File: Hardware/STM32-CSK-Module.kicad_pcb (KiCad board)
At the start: 2 copper layers, 7 parts

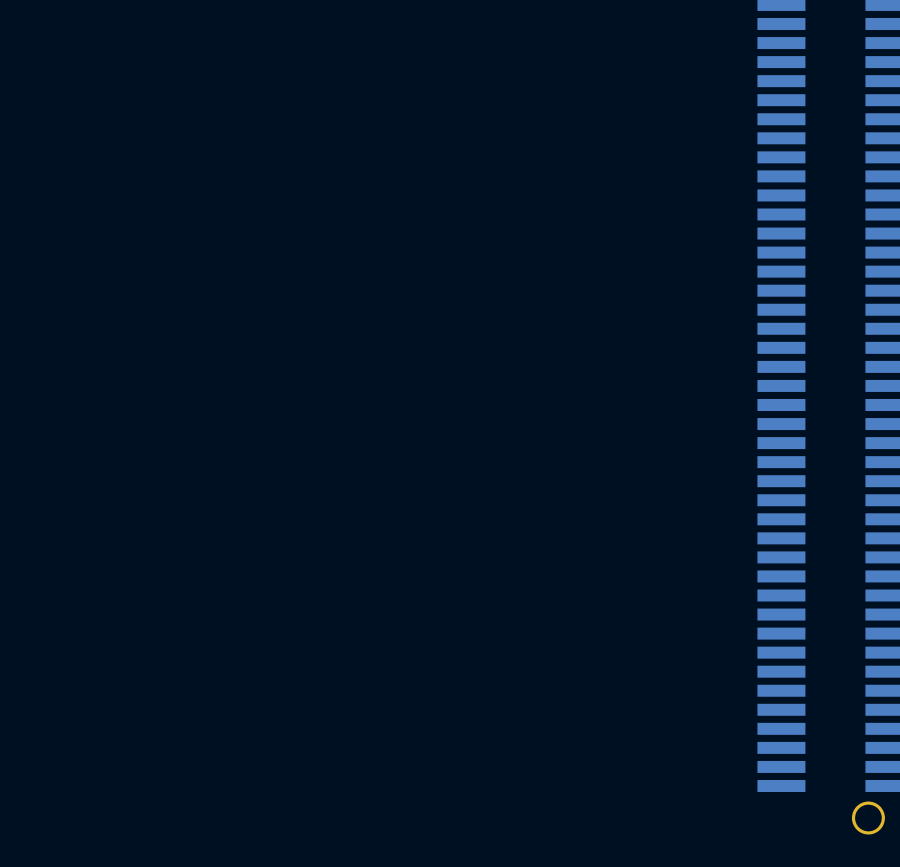
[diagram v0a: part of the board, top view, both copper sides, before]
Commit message: Add MCU
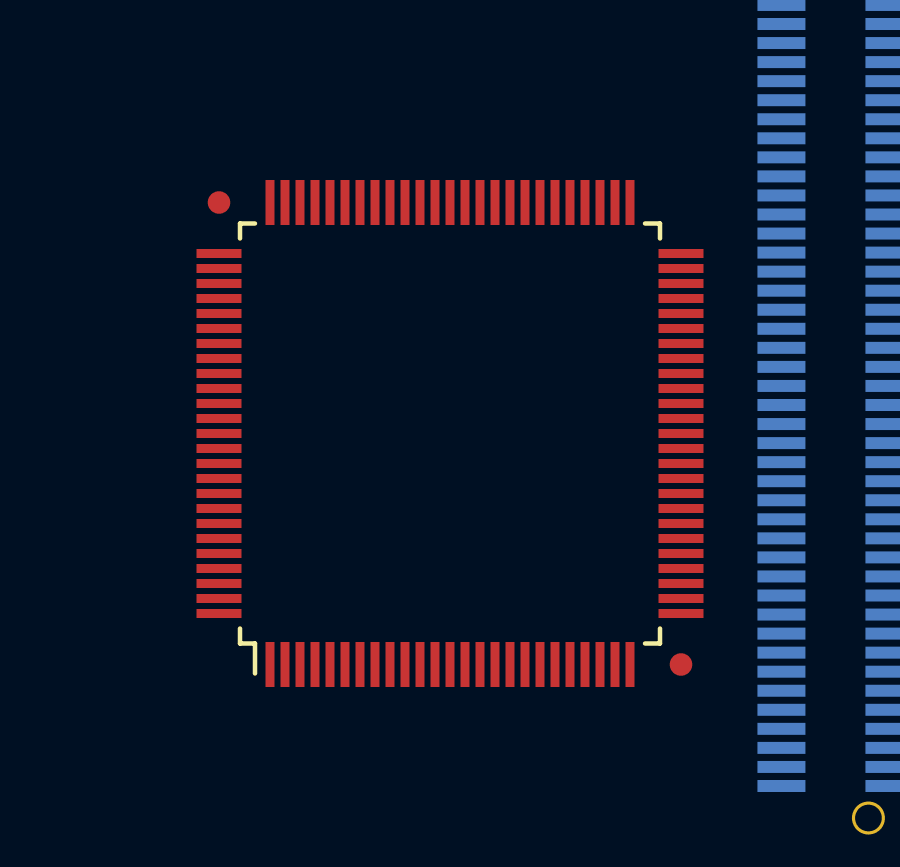
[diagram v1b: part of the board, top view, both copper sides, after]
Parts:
- added U1: STM32F4X7V, QFP50P1600X1600-100N, F.Cu at (209.0, 120.0)
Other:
- board text added: "Connector keep out"

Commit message: Migrate to new KiCad
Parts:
- added C1: 0.1uF, Capacitors:CAPC1608N, F.Cu at (208.4, 156.5)
- added C10: 0.1uF, Capacitors:CAPC1608N, F.Cu at (222.8, 156.5)
- added C11: 2.2uF, Capacitors:CAPC1608N, F.Cu at (216.9, 161.7)
- added C12: 0.1uF, Capacitors:CAPC1608N, F.Cu at (213.2, 166.9)
- added C13: 0.1uF, Capacitors:CAPC1608N, F.Cu at (221.7, 161.7)
- added C2: 0.1uF, Capacitors:CAPC1608N, F.Cu at (213.9, 151.3)
- added C3: 1uF, Capacitors:CAPC1608N, F.Cu at (207.8, 161.7)
- added C4: 4.7uF, Capacitors:CAPC1608N, F.Cu at (218.7, 151.3)
- added C5: 0.1uF, Capacitors:CAPC1608N, F.Cu at (213.2, 156.5)
- added C6: 0.1uF, Capacitors:CAPC1608N, F.Cu at (208.4, 166.9)
- added C7: 0.1uF, Capacitors:CAPC1608N, F.Cu at (218.0, 156.5)
- added C8: 0.1uF, Capacitors:CAPC1608N, F.Cu at (212.1, 161.7)
- added C9: 2.2uF, Capacitors:CAPC1608N, F.Cu at (223.5, 151.3)
- added FB1: Ferrite, Inductors:INDC1608N, F.Cu at (208.8, 151.3)
- added R1: 10k, Resistors:RESC1608N, F.Cu at (217.4, 166.9)
- H1: value CUBESAT-PSPM -> Conn_Cubesat-PPM; footprint CONN-LSS-150 -> Connectors:Conn_Samtec-LSS-150
- MECH-HOLE220 (x6): footprint MECH-HOLE220 -> Mechanical:MTGP575H254
- U1: value STM32F4X7V -> STM32F417VGT; footprint QFP50P1600X1600-100N -> QFP:QFP50P1600X1600-100N
- moved U1 39.5 mm to (197.0, 157.6)
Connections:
- H1 pad 1: (no net) -> Net-(H1-Pad1)
- H1 pad 10: (no net) -> Net-(H1-Pad10)
- H1 pad 100: (no net) -> Net-(H1-Pad100)
- H1 pad 11: (no net) -> Net-(H1-Pad11)
- H1 pad 12: (no net) -> Net-(H1-Pad12)
- H1 pad 13: (no net) -> Net-(H1-Pad13)
- H1 pad 14: (no net) -> Net-(H1-Pad14)
- H1 pad 15: (no net) -> Net-(H1-Pad15)
- H1 pad 16: (no net) -> Net-(H1-Pad16)
- H1 pad 17: (no net) -> Net-(H1-Pad17)
- H1 pad 18: (no net) -> Net-(H1-Pad18)
- H1 pad 19: (no net) -> Net-(H1-Pad19)
- H1 pad 2: (no net) -> Net-(H1-Pad2)
- H1 pad 20: (no net) -> Net-(H1-Pad20)
- H1 pad 21: (no net) -> Net-(H1-Pad21)
- H1 pad 22: (no net) -> Net-(H1-Pad22)
- H1 pad 23: (no net) -> Net-(H1-Pad23)
- H1 pad 24: (no net) -> Net-(H1-Pad24)
- H1 pad 25: (no net) -> Net-(H1-Pad25)
- H1 pad 26: (no net) -> Net-(H1-Pad26)
- H1 pad 27: (no net) -> Net-(H1-Pad27)
- H1 pad 28: (no net) -> Net-(H1-Pad28)
- H1 pad 29: (no net) -> Net-(H1-Pad29)
- H1 pad 3: (no net) -> Net-(H1-Pad3)
- H1 pad 30: (no net) -> Net-(H1-Pad30)
- H1 pad 31: (no net) -> Net-(H1-Pad31)
- H1 pad 32: (no net) -> Net-(H1-Pad32)
- H1 pad 33: (no net) -> Net-(H1-Pad33)
- H1 pad 34: (no net) -> Net-(H1-Pad34)
- H1 pad 35: (no net) -> Net-(H1-Pad35)
- H1 pad 36: (no net) -> Net-(H1-Pad36)
- H1 pad 37: (no net) -> Net-(H1-Pad37)
- H1 pad 38: (no net) -> Net-(H1-Pad38)
- H1 pad 39: (no net) -> Net-(H1-Pad39)
- H1 pad 4: (no net) -> Net-(H1-Pad4)
- H1 pad 40: (no net) -> Net-(H1-Pad40)
- H1 pad 41: (no net) -> Net-(H1-Pad41)
- H1 pad 42: (no net) -> Net-(H1-Pad42)
- H1 pad 43: (no net) -> Net-(H1-Pad43)
- H1 pad 44: (no net) -> Net-(H1-Pad44)
- H1 pad 45: (no net) -> Net-(H1-Pad45)
- H1 pad 46: (no net) -> Net-(H1-Pad46)
- H1 pad 47: (no net) -> Net-(H1-Pad47)
- H1 pad 48: (no net) -> Net-(H1-Pad48)
- H1 pad 49: (no net) -> Net-(H1-Pad49)
- H1 pad 5: (no net) -> Net-(H1-Pad5)
- H1 pad 50: (no net) -> Net-(H1-Pad50)
- H1 pad 51: (no net) -> Net-(H1-Pad51)
- H1 pad 52: (no net) -> Net-(H1-Pad52)
- H1 pad 53: (no net) -> Net-(H1-Pad53)
- H1 pad 54: (no net) -> Net-(H1-Pad54)
- H1 pad 55: (no net) -> Net-(H1-Pad55)
- H1 pad 56: (no net) -> Net-(H1-Pad56)
- H1 pad 57: (no net) -> GND
- H1 pad 58: (no net) -> GND
- H1 pad 59: (no net) -> Net-(H1-Pad59)
- H1 pad 6: (no net) -> Net-(H1-Pad6)
- H1 pad 60: (no net) -> Net-(H1-Pad60)
- H1 pad 61: (no net) -> Net-(H1-Pad61)
- H1 pad 62: (no net) -> Net-(H1-Pad62)
- H1 pad 63: (no net) -> Net-(H1-Pad63)
- H1 pad 64: (no net) -> Net-(H1-Pad64)
- H1 pad 65: (no net) -> Net-(H1-Pad65)
- H1 pad 66: (no net) -> Net-(H1-Pad66)
- H1 pad 67: (no net) -> Net-(H1-Pad67)
- H1 pad 68: (no net) -> Net-(H1-Pad68)
- H1 pad 69: (no net) -> Net-(H1-Pad69)
- H1 pad 7: (no net) -> Net-(H1-Pad7)
- H1 pad 70: (no net) -> Net-(H1-Pad70)
- H1 pad 71: (no net) -> Net-(H1-Pad71)
- H1 pad 72: (no net) -> Net-(H1-Pad72)
- H1 pad 73: (no net) -> Net-(H1-Pad73)
- H1 pad 74: (no net) -> Net-(H1-Pad74)
- H1 pad 75: (no net) -> Net-(H1-Pad75)
- H1 pad 76: (no net) -> Net-(H1-Pad76)
- H1 pad 77: (no net) -> Net-(H1-Pad77)
- H1 pad 78: (no net) -> Net-(H1-Pad78)
- H1 pad 79: (no net) -> Net-(H1-Pad79)
- H1 pad 8: (no net) -> Net-(H1-Pad8)
- H1 pad 80: (no net) -> Net-(H1-Pad80)
- H1 pad 81: (no net) -> Net-(H1-Pad81)
- H1 pad 82: (no net) -> Net-(H1-Pad82)
- H1 pad 83: (no net) -> Net-(H1-Pad83)
- H1 pad 84: (no net) -> Net-(H1-Pad84)
- H1 pad 85: (no net) -> Net-(H1-Pad85)
- H1 pad 86: (no net) -> Net-(H1-Pad86)
- H1 pad 87: (no net) -> Net-(H1-Pad87)
- H1 pad 88: (no net) -> Net-(H1-Pad88)
- H1 pad 89: (no net) -> Net-(H1-Pad89)
- H1 pad 9: (no net) -> Net-(H1-Pad9)
- H1 pad 90: (no net) -> Net-(H1-Pad90)
- H1 pad 91: (no net) -> Net-(H1-Pad91)
- H1 pad 92: (no net) -> Net-(H1-Pad92)
- H1 pad 93: (no net) -> Net-(H1-Pad93)
- H1 pad 94: (no net) -> Net-(H1-Pad94)
- H1 pad 95: (no net) -> Net-(H1-Pad95)
- H1 pad 96: (no net) -> Net-(H1-Pad96)
- H1 pad 97: (no net) -> Net-(H1-Pad97)
- H1 pad 98: (no net) -> Net-(H1-Pad98)
- H1 pad 99: (no net) -> Net-(H1-Pad99)
- U1 pad 1: (no net) -> Net-(U1-Pad1)
- U1 pad 10: (no net) -> GND
- U1 pad 100: (no net) -> +3V3
- U1 pad 11: (no net) -> +3V3
- U1 pad 12: (no net) -> Net-(U1-Pad12)
- U1 pad 13: (no net) -> Net-(U1-Pad13)
- U1 pad 14: (no net) -> /~RST
- U1 pad 15: (no net) -> Net-(U1-Pad15)
- U1 pad 16: (no net) -> Net-(U1-Pad16)
- U1 pad 17: (no net) -> Net-(U1-Pad17)
- U1 pad 18: (no net) -> Net-(U1-Pad18)
- U1 pad 19: (no net) -> +3V3
- U1 pad 2: (no net) -> Net-(U1-Pad2)
- U1 pad 20: (no net) -> GND
- U1 pad 21: (no net) -> /VDDA
- U1 pad 22: (no net) -> /VDDA
- U1 pad 23: (no net) -> Net-(U1-Pad23)
- U1 pad 24: (no net) -> Net-(U1-Pad24)
- U1 pad 25: (no net) -> Net-(U1-Pad25)
- U1 pad 26: (no net) -> Net-(U1-Pad26)
- U1 pad 27: (no net) -> GND
- U1 pad 28: (no net) -> +3V3
- U1 pad 29: (no net) -> Net-(U1-Pad29)
- U1 pad 3: (no net) -> Net-(U1-Pad3)
- U1 pad 30: (no net) -> Net-(U1-Pad30)
- U1 pad 31: (no net) -> Net-(U1-Pad31)
- U1 pad 32: (no net) -> Net-(U1-Pad32)
- U1 pad 33: (no net) -> Net-(U1-Pad33)
- U1 pad 34: (no net) -> Net-(U1-Pad34)
- U1 pad 35: (no net) -> Net-(U1-Pad35)
- U1 pad 36: (no net) -> Net-(U1-Pad36)
- U1 pad 37: (no net) -> Net-(U1-Pad37)
- U1 pad 38: (no net) -> Net-(U1-Pad38)
- U1 pad 39: (no net) -> Net-(U1-Pad39)
- U1 pad 4: (no net) -> Net-(U1-Pad4)
- U1 pad 40: (no net) -> Net-(U1-Pad40)
- U1 pad 41: (no net) -> Net-(U1-Pad41)
- U1 pad 42: (no net) -> Net-(U1-Pad42)
- U1 pad 43: (no net) -> Net-(U1-Pad43)
- U1 pad 44: (no net) -> Net-(U1-Pad44)
- U1 pad 45: (no net) -> Net-(U1-Pad45)
- U1 pad 46: (no net) -> Net-(U1-Pad46)
- U1 pad 47: (no net) -> Net-(U1-Pad47)
- U1 pad 48: (no net) -> Net-(U1-Pad48)
- U1 pad 49: (no net) -> /VCAP1
- U1 pad 5: (no net) -> Net-(U1-Pad5)
- U1 pad 50: (no net) -> +3V3
- U1 pad 51: (no net) -> Net-(U1-Pad51)
- U1 pad 52: (no net) -> Net-(U1-Pad52)
- U1 pad 53: (no net) -> Net-(U1-Pad53)
- U1 pad 54: (no net) -> Net-(U1-Pad54)
- U1 pad 55: (no net) -> Net-(U1-Pad55)
- U1 pad 56: (no net) -> Net-(U1-Pad56)
- U1 pad 57: (no net) -> Net-(U1-Pad57)
- U1 pad 58: (no net) -> Net-(U1-Pad58)
- U1 pad 59: (no net) -> Net-(U1-Pad59)
- U1 pad 6: (no net) -> /VBAT
- U1 pad 60: (no net) -> Net-(U1-Pad60)
- U1 pad 61: (no net) -> Net-(U1-Pad61)
- U1 pad 62: (no net) -> Net-(U1-Pad62)
- U1 pad 63: (no net) -> Net-(U1-Pad63)
- U1 pad 64: (no net) -> Net-(U1-Pad64)
- U1 pad 65: (no net) -> Net-(U1-Pad65)
- U1 pad 66: (no net) -> Net-(U1-Pad66)
- U1 pad 67: (no net) -> Net-(U1-Pad67)
- U1 pad 68: (no net) -> Net-(U1-Pad68)
- U1 pad 69: (no net) -> Net-(U1-Pad69)
- U1 pad 7: (no net) -> Net-(U1-Pad7)
- U1 pad 70: (no net) -> Net-(U1-Pad70)
- U1 pad 71: (no net) -> Net-(U1-Pad71)
- U1 pad 72: (no net) -> Net-(U1-Pad72)
- U1 pad 73: (no net) -> /VCAP2
- U1 pad 74: (no net) -> GND
- U1 pad 75: (no net) -> +3V3
- U1 pad 76: (no net) -> Net-(U1-Pad76)
- U1 pad 77: (no net) -> Net-(U1-Pad77)
- U1 pad 78: (no net) -> Net-(U1-Pad78)
- U1 pad 79: (no net) -> Net-(U1-Pad79)
- U1 pad 8: (no net) -> Net-(U1-Pad8)
- U1 pad 80: (no net) -> Net-(U1-Pad80)
- U1 pad 81: (no net) -> Net-(U1-Pad81)
- U1 pad 82: (no net) -> Net-(U1-Pad82)
- U1 pad 83: (no net) -> Net-(U1-Pad83)
- U1 pad 84: (no net) -> Net-(U1-Pad84)
- U1 pad 85: (no net) -> Net-(U1-Pad85)
- U1 pad 86: (no net) -> Net-(U1-Pad86)
- U1 pad 87: (no net) -> Net-(U1-Pad87)
- U1 pad 88: (no net) -> Net-(U1-Pad88)
- U1 pad 89: (no net) -> Net-(U1-Pad89)
- U1 pad 9: (no net) -> Net-(U1-Pad9)
- U1 pad 90: (no net) -> Net-(U1-Pad90)
- U1 pad 91: (no net) -> Net-(U1-Pad91)
- U1 pad 92: (no net) -> Net-(U1-Pad92)
- U1 pad 93: (no net) -> Net-(U1-Pad93)
- U1 pad 94: (no net) -> /BOOT
- U1 pad 95: (no net) -> Net-(U1-Pad95)
- U1 pad 96: (no net) -> Net-(U1-Pad96)
- U1 pad 97: (no net) -> Net-(U1-Pad97)
- U1 pad 98: (no net) -> Net-(U1-Pad98)
- U1 pad 99: (no net) -> GND

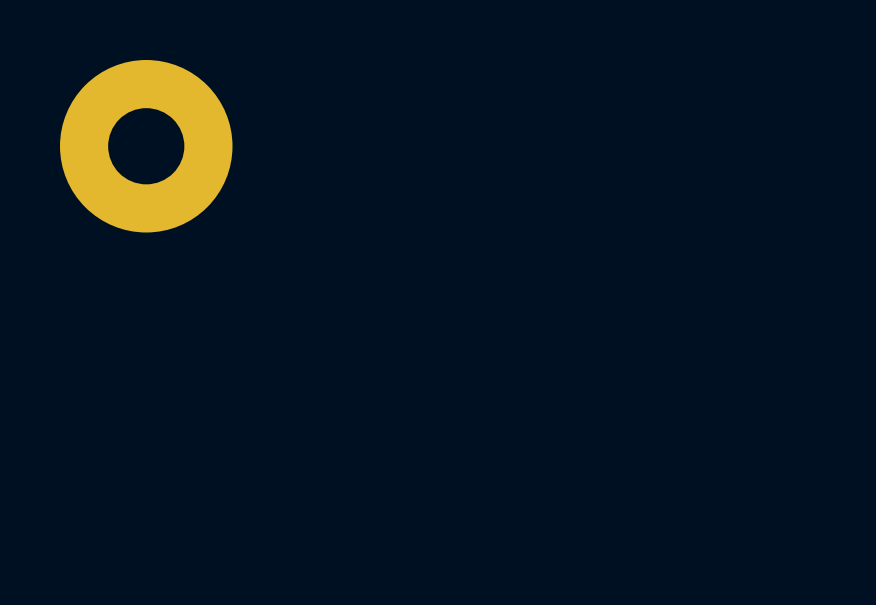
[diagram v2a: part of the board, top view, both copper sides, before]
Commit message: Add crystals and programmer
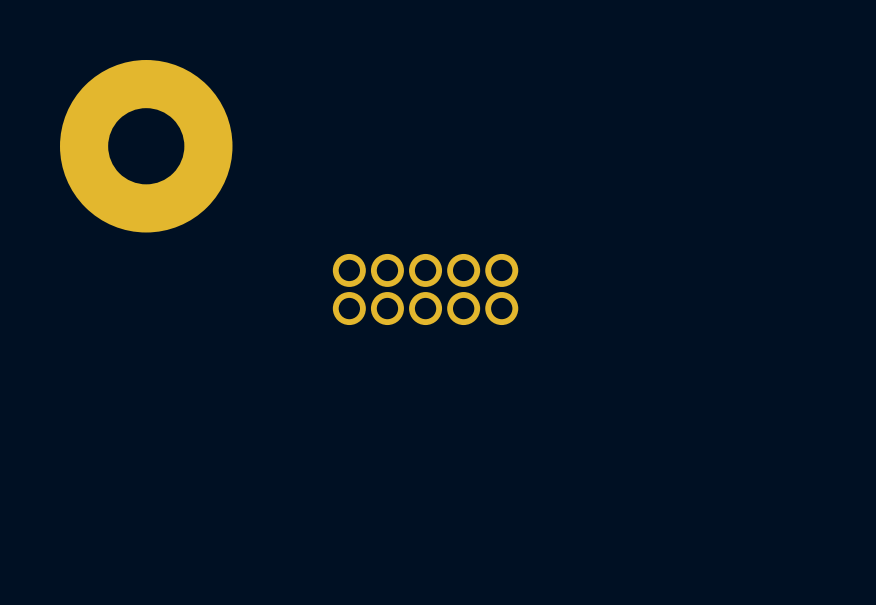
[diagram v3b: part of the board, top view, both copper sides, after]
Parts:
- added J1: Conn_Cortex-JTAG-10, Connectors:Conn_Samtec-FTSH-105-D-RA-K, B.Cu at (196.8, 105.4)
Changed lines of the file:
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@@
 (kicad_pcb (version 4) (host pcbnew "(2014-12-20 BZR 5331)-product")
   (general
-    (links 42)
-    (no_connects 42)
+    (links 47)
+    (no_connects 47)
     (area 178.671 92.899999 239.100001 188.365001)
     (thickness 1.6)
@@
     (tracks 0)
     (zones 0)
-    (modules 23)
-    (nets 189)
+    (modules 24)
+    (nets 193)
   )
   (page A3)
@@
   (net 187 "Net-(U1-Pad97)")
   (net 188 "Net-(U1-Pad98)")
+  (net 189 "Net-(J1-Pad8)")
+  (net 190 "Net-(J1-Pad6)")
+  (net 191 /SWCLK)
+  (net 192 /SWDIO)
   (net_class Default "This is the default net class."
     (clearance 0.254)
@@
     (add_net +3V3)
     (add_net /BOOT)
+    (add_net /SWCLK)
+    (add_net /SWDIO)
     (add_net /VBAT)
     (add_net /VCAP1)
@@
     (add_net "Net-(H1-Pad98)")
     (add_net "Net-(H1-Pad99)")
+    (add_net "Net-(J1-Pad6)")
+    (add_net "Net-(J1-Pad8)")
     (add_net "Net-(U1-Pad1)")
     (add_net "Net-(U1-Pad12)")
@@
     (pad 1 thru_hole circle (at 0 0) (size 5.75 5.75) (drill 2.54) (layers *.Cu *.Mask))
   )
+  (module Connectors:Conn_Samtec-FTSH-105-D-RA-K (layer B.Cu)
+    (at 196.85 105.41)
+    (descr "0.05\" Header Right Angle 2x5")
+    (fp_text reference J1 (at -2.54 1.905) (layer B.SilkS)
+      (effects (font (size 1 1) (thickness 0.15)) (justify mirror))
+    )
+    (fp_text value Conn_Cortex-JTAG-10 (at -2.54 3.175) (layer B.SilkS) hide
+      (effects (font (size 1 1) (thickness 0.15)) (justify mirror))
+    )
+    (fp_line (start -5.969 -8.382) (end -5.969 0.889) (layer B.CrtYd) (width 0.15))
+    (fp_line (start -5.969 0.889) (end 0.889 0.889) (layer B.CrtYd) (width 0.15))
+    (fp_line (start 0.889 0.889) (end 0.889 -8.382) (layer B.CrtYd) (width 0.15))
+    (fp_line (start 0.889 -8.382) (end -5.969 -8.382) (layer B.CrtYd) (width 0.15))
+    (fp_line (start 0.762 0.635) (end 0.762 -8.255) (layer B.SilkS) (width 0.15))
+    (fp_line (start -5.842 -8.255) (end 0.762 -8.255) (layer B.SilkS) (width 0.15))
+    (fp_line (start -5.842 -8.255) (end -5.842 -2.413) (layer B.SilkS) (width 0.15))
+    (fp_line (start -5.715 -5.08) (end 0.635 -5.08) (layer B.Fab) (width 0.15))
+    (fp_line (start -5.715 -2.54) (end 0.635 -2.54) (layer B.Fab) (width 0.15))
+    (fp_line (start 0.635 -2.54) (end 0.635 -8.1) (layer B.Fab) (width 0.15))
+    (fp_line (start 0.635 -8.1) (end -5.715 -8.1) (layer B.Fab) (width 0.15))
+    (fp_line (start -5.715 -8.1) (end -5.715 -2.54) (layer B.Fab) (width 0.15))
+    (pad 9 thru_hole circle (at -5.08 0) (size 1.1 1.1) (drill 0.71) (layers *.Cu *.Mask)
+      (net 2 GND))
+    (pad 10 thru_hole circle (at -5.08 -1.27) (size 1.1 1.1) (drill 0.71) (layers *.Cu *.Mask)
+      (net 4 /~RST))
+    (pad 7 thru_hole circle (at -3.81 0) (size 1.1 1.1) (drill 0.71) (layers *.Cu *.Mask))
+    (pad 8 thru_hole circle (at -3.81 -1.27) (size 1.1 1.1) (drill 0.71) (layers *.Cu *.Mask)
+      (net 189 "Net-(J1-Pad8)"))
+    (pad 5 thru_hole circle (at -2.54 0) (size 1.1 1.1) (drill 0.71) (layers *.Cu *.Mask)
+      (net 2 GND))
+    (pad 6 thru_hole circle (at -2.54 -1.27) (size 1.1 1.1) (drill 0.71) (layers *.Cu *.Mask)
+      (net 190 "Net-(J1-Pad6)"))
+    (pad 3 thru_hole circle (at -1.27 0) (size 1.1 1.1) (drill 0.71) (layers *.Cu *.Mask)
+      (net 2 GND))
+    (pad 4 thru_hole circle (at -1.27 -1.27) (size 1.1 1.1) (drill 0.71) (layers *.Cu *.Mask)
+      (net 191 /SWCLK))
+    (pad 1 thru_hole circle (at 0 0) (size 1.1 1.1) (drill 0.71) (layers *.Cu *.Mask)
+      (net 3 +3V3))
+    (pad 2 thru_hole circle (at 0 -1.27) (size 1.1 1.1) (drill 0.71) (layers *.Cu *.Mask)
+      (net 192 /SWDIO))
+    (model Connectors/Conn_Samtec-FTSH-105-D-RA-K.wrl
+      (at (xyz 0 0 0))
+      (scale (xyz 0.393701 0.393701 0.393701))
+      (rotate (xyz 0 0 0))
+    )
+  )
   (gr_text "Connector keep out" (at 222 95) (layer Cmts.User)

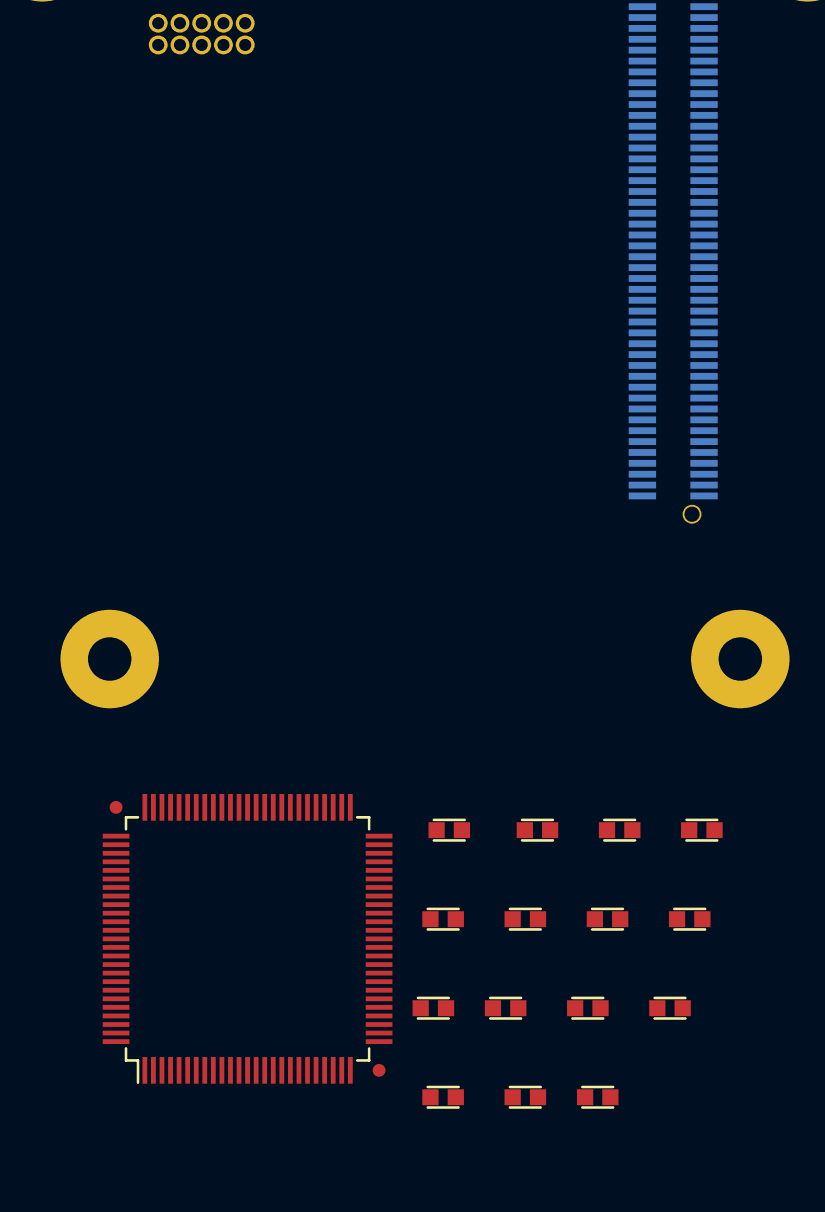
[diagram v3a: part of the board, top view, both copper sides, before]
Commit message: Peripheral pin mapping
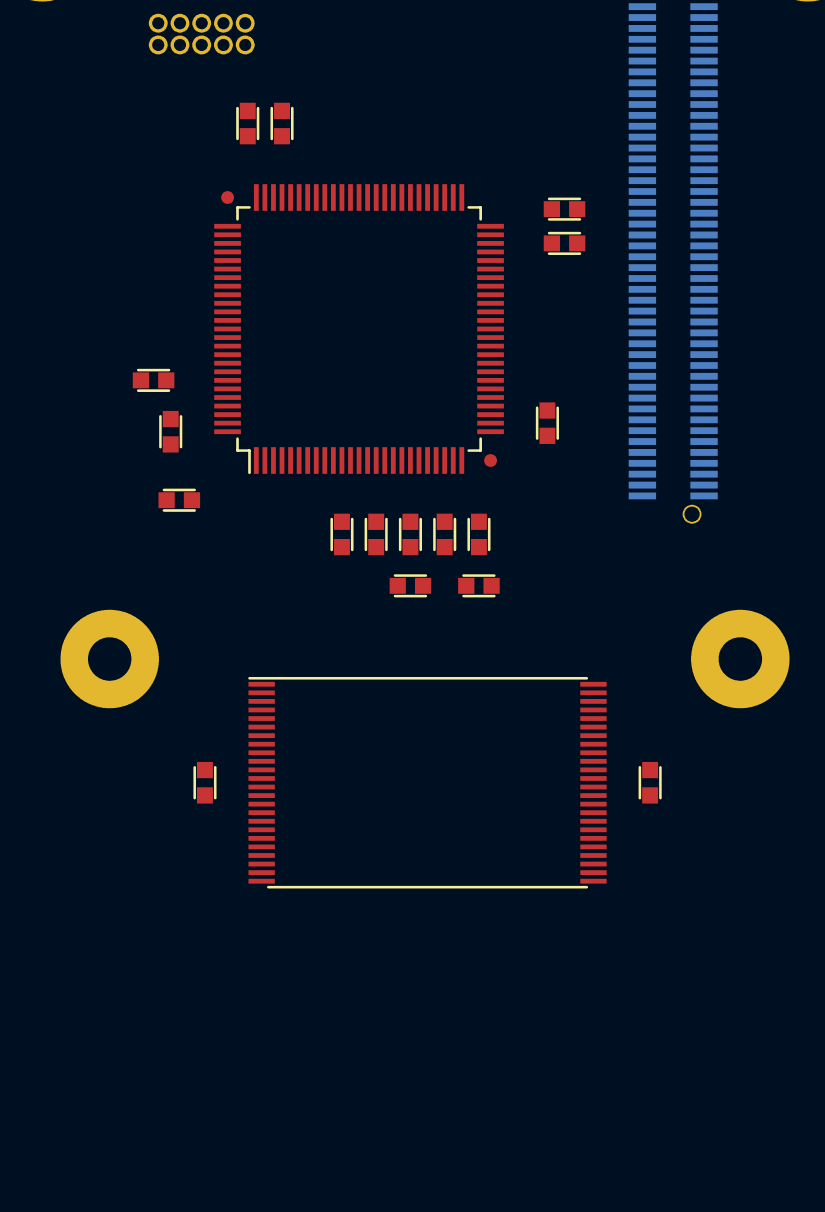
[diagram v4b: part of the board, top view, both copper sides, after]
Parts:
- added C18: 0.1uF, Capacitors:CAPC1608N, F.Cu at (194.5, 148.5)
- added C19: 0.1uF, Capacitors:CAPC1608N, F.Cu at (220.5, 148.5)
- added U2: S34ML02G104T, SOP:SOP50P2000-48N, F.Cu at (207.5, 148.5)
- moved C12 59.1 mm to (197.0, 110.0), turned to 90 degrees
- moved C11 54.7 mm to (199.0, 110.0), turned to 90 degrees
- moved R1 49.3 mm to (191.5, 125.0), turned to 180 degrees
- moved C13 44.5 mm to (192.5, 128.0), turned to 90 degrees
- moved C10 42.1 mm to (215.5, 115.0)
- moved U1 36.2 mm to (203.5, 122.0)
- moved C9 35.2 mm to (215.5, 117.0)
- moved C8 34.3 mm to (214.5, 127.5), turned to 270 degrees
- moved C6 32.9 mm to (206.5, 134.0), turned to 270 degrees
- moved C4 32.1 mm to (193.0, 132.0)
- moved C7 26.2 mm to (204.5, 134.0), turned to 270 degrees
- moved C5 24.9 mm to (202.5, 134.0), turned to 270 degrees
- moved C3 24.8 mm to (210.5, 137.0)
- moved C1 22.5 mm to (208.5, 134.0), turned to 270 degrees
- moved C2 17.6 mm to (210.5, 134.0), turned to 270 degrees
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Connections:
- net Net-(U1-Pad12) renamed /OSCI
- net Net-(U1-Pad13) renamed /OSCO
- net Net-(U1-Pad23) renamed /USART2_CTS
- net Net-(U1-Pad24) renamed /USART2_RTS
- net Net-(U1-Pad25) renamed /USART2_TX
- net Net-(U1-Pad26) renamed /USART2_RX
- net Net-(U1-Pad47) renamed /I2C2_SCL
- net Net-(U1-Pad48) renamed /I2C2_SDA
- net Net-(U1-Pad51) renamed /~SPI2_SS
- net Net-(U1-Pad52) renamed /SPI2_SCK
- net Net-(U1-Pad53) renamed /SPI2_MISO
- net Net-(U1-Pad54) renamed /SPI2_MOSI
- net Net-(U1-Pad66) renamed /I2C3_SDA
- net Net-(U1-Pad67) renamed /I2C3_SCL
- net Net-(U1-Pad70) renamed /USART1_CTS
- net Net-(U1-Pad71) renamed /USART1_RTS
- net Net-(U1-Pad77) renamed /~SPI1_SS
- net Net-(U1-Pad8) renamed /SOSCI
- net Net-(U1-Pad89) renamed /SPI1_SCK
- net Net-(U1-Pad9) renamed /SOSCO
- net Net-(U1-Pad90) renamed /SPI1_MISO
- net Net-(U1-Pad91) renamed /SPI1_MOSI
- net Net-(U1-Pad92) renamed /USART1_TX
- net Net-(U1-Pad93) renamed /USART1_RX
- net Net-(U1-Pad95) renamed /I2C1_SCL
- net Net-(U1-Pad96) renamed /I2C1_SDA
- U1 pad 38: Net-(U1-Pad38) -> /FSMC4
- U1 pad 39: Net-(U1-Pad39) -> /FSMC5
- U1 pad 40: Net-(U1-Pad40) -> /FSMC6
- U1 pad 41: Net-(U1-Pad41) -> /FSMC7
- U1 pad 42: Net-(U1-Pad42) -> /FSMC8
- U1 pad 43: Net-(U1-Pad43) -> /FSMC9
- U1 pad 44: Net-(U1-Pad44) -> /FSMC10
- U1 pad 45: Net-(U1-Pad45) -> /FSMC11
- U1 pad 46: Net-(U1-Pad46) -> /FSMC12
- U1 pad 55: Net-(U1-Pad55) -> /FSMC13
- U1 pad 56: Net-(U1-Pad56) -> /FSMC14
- U1 pad 57: Net-(U1-Pad57) -> /FSMC15
- U1 pad 58: Net-(U1-Pad58) -> /FSMC_CLE
- U1 pad 59: Net-(U1-Pad59) -> /FSMC_ALE
- U1 pad 61: Net-(U1-Pad61) -> /FSMC0
- U1 pad 62: Net-(U1-Pad62) -> /FSMC1
- U1 pad 72: Net-(U1-Pad72) -> /SWDIO
- U1 pad 76: Net-(U1-Pad76) -> /SWCLK
- U1 pad 81: Net-(U1-Pad81) -> /FSMC2
- U1 pad 82: Net-(U1-Pad82) -> /FSMC3
- U1 pad 85: Net-(U1-Pad85) -> /~FSMC_OE
- U1 pad 86: Net-(U1-Pad86) -> /~FSMC_WE
- U1 pad 87: Net-(U1-Pad87) -> /~FSMC_WAIT
- U1 pad 88: Net-(U1-Pad88) -> /~FSMC_CE
